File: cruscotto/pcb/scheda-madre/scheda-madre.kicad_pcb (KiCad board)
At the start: 2 copper layers, 178.7 x 74 mm, 13 parts, among them J1 Micro-Fit 2x12 verso auto (D-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

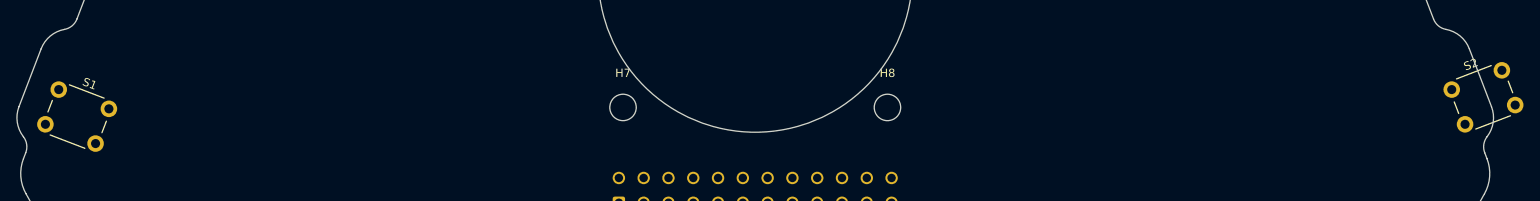
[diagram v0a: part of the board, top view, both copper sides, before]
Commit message: fix(pcb): switches centred under the original buttons and rotated with pins parallel to the edge
The footprint origin is pin 1, so the right switch body fell outside the board. DRC 0 violations; courtyard corners overhang the edge by ~0.5 mm.

Co-Authored-By: Claude Opus 5.5 <noreply@anthropic.com>
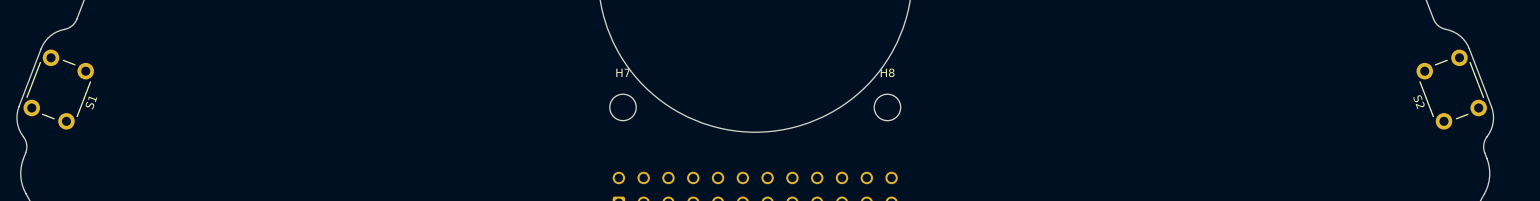
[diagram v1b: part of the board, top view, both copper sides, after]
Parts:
- moved S2 3.95 mm to (231.8, 122.7), turned to 111 degrees
- moved S1 3.95 mm to (67.5, 116.6), turned to -111 degrees

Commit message: feat(pcb): netlist import and preliminary block placement of all 139 parts on both sides
Nets from the schematic via kicad-cli; placement checks outline, holes, fan, overlaps and through-hole pins on both faces. ESP32 radio unused: body-only courtyard. Design rules in the project file. DRC: only unrouted connections.

Co-Authored-By: Claude Opus 5.5 <noreply@anthropic.com>
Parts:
- added BT1: CR2032, BatteryHolder_Keystone_3034_1x20mm, B.Cu at (182.1, 89.5)
- added C1: 100nF 100V, C_0805_2012Metric_Pad1.18x1.45mm_HandSolder, F.Cu at (111.6, 75.5)
- added C10: 39pF, C_0805_2012Metric_Pad1.18x1.45mm_HandSolder, F.Cu at (111.6, 116.0)
- added C11: 2.2uF 100V, C_1210_3225Metric_Pad1.33x2.70mm_HandSolder, F.Cu at (92.5, 111.6)
- added C12: 220nF 100V, C_0805_2012Metric_Pad1.18x1.45mm_HandSolder, F.Cu at (111.6, 119.0)
- added C13: 1uF, C_0805_2012Metric_Pad1.18x1.45mm_HandSolder, F.Cu at (111.6, 122.0)
- added C14: 100nF, C_0805_2012Metric_Pad1.18x1.45mm_HandSolder, F.Cu at (126.1, 122.5)
- added C15: 22uF 10V, C_1206_3216Metric_Pad1.33x1.80mm_HandSolder, F.Cu at (86.5, 111.2)
- added C16: 22uF 10V, C_1206_3216Metric_Pad1.33x1.80mm_HandSolder, F.Cu at (80.5, 112.7)
- added C17: 22uF 10V, C_1206_3216Metric_Pad1.33x1.80mm_HandSolder, F.Cu at (111.0, 113.2)
- added C18: 100nF, C_0805_2012Metric_Pad1.18x1.45mm_HandSolder, F.Cu at (121.6, 122.5)
- added C19: 100nF, C_0805_2012Metric_Pad1.18x1.45mm_HandSolder, F.Cu at (117.1, 122.5)
- added C2: 100nF 25V, C_0805_2012Metric_Pad1.18x1.45mm_HandSolder, F.Cu at (126.1, 86.0)
- added C20: 22uF 10V, C_1206_3216Metric_Pad1.33x1.80mm_HandSolder, F.Cu at (145.0, 79.2)
- added C21: 100nF, C_0805_2012Metric_Pad1.18x1.45mm_HandSolder, F.Cu at (163.6, 79.5)
- added C22: 1uF, C_0805_2012Metric_Pad1.18x1.45mm_HandSolder, F.Cu at (192.1, 80.0)
- added C23: 100nF, C_0805_2012Metric_Pad1.18x1.45mm_HandSolder, F.Cu at (150.1, 80.5)
- added C24: 100nF, C_0805_2012Metric_Pad1.18x1.45mm_HandSolder, F.Cu at (168.1, 80.5)
- added C25: 1uF, C_0805_2012Metric_Pad1.18x1.45mm_HandSolder, F.Cu at (149.6, 70.0)
- added C26: 1uF, C_0805_2012Metric_Pad1.18x1.45mm_HandSolder, F.Cu at (154.1, 70.0)
- added C27: 100nF, C_0805_2012Metric_Pad1.18x1.45mm_HandSolder, F.Cu at (170.6, 70.0)
- added C28: 100nF, C_0805_2012Metric_Pad1.18x1.45mm_HandSolder, F.Cu at (218.6, 109.0)
- added C29: 10uF 16V, CP_Elec_4x5.4, F.Cu at (212.6, 106.4)
- added C3: 220uF 50V, CP_Radial_D10.0mm_P5.00mm, B.Cu at (93.7, 96.3)
- added C30: 100nF, C_0805_2012Metric_Pad1.18x1.45mm_HandSolder, F.Cu at (216.6, 112.0)
- added C31: 1uF, C_0805_2012Metric_Pad1.18x1.45mm_HandSolder, F.Cu at (211.1, 113.5)
- added C32: 1uF, C_0805_2012Metric_Pad1.18x1.45mm_HandSolder, F.Cu at (180.6, 114.0)
- added C33: 100nF, C_0805_2012Metric_Pad1.18x1.45mm_HandSolder, F.Cu at (180.1, 81.5)
- added C34: 100nF, C_0805_2012Metric_Pad1.18x1.45mm_HandSolder, B.Cu at (111.6, 75.5)
- added C35: 10uF, C_1206_3216Metric_Pad1.33x1.80mm_HandSolder, F.Cu at (158.5, 79.7)
- added C36: 100nF, C_0805_2012Metric_Pad1.18x1.45mm_HandSolder, F.Cu at (184.6, 81.5)
- added C4: 2.2uF 100V, C_1210_3225Metric_Pad1.33x2.70mm_HandSolder, F.Cu at (107.0, 79.6)
- added C5: 2.2uF 100V, C_1210_3225Metric_Pad1.33x2.70mm_HandSolder, F.Cu at (95.0, 88.1)
- added C6: 100nF, C_0805_2012Metric_Pad1.18x1.45mm_HandSolder, F.Cu at (126.1, 89.0)
- added C7: 47uF 10V, C_1210_3225Metric_Pad1.33x2.70mm_HandSolder, F.Cu at (82.5, 96.6)
- added C8: 47uF 10V, C_1210_3225Metric_Pad1.33x2.70mm_HandSolder, F.Cu at (98.5, 110.6)
- added C9: 6.8nF, C_0805_2012Metric_Pad1.18x1.45mm_HandSolder, F.Cu at (126.1, 99.0)
- added D1: SMCJ26CA, D_SMC, F.Cu at (104.6, 93.9)
- added D10: NUP2105L, SOT-23, F.Cu at (185.0, 110.2)
- added D11: 1N4148W, D_SOD-123, B.Cu at (94.1, 88.2)
- added D12: 1N4148W, D_SOD-123, B.Cu at (185.6, 76.2)
- added D13: B340A, D_SMA, F.Cu at (186.0, 77.8)
- added D2: B560C, D_SMC, F.Cu at (104.6, 101.4)
- added D3: 1N4148W, D_SOD-123, F.Cu at (105.1, 113.2)
- added D4: BAT54J, D_SOD-323F, F.Cu at (125.9, 102.0)
- added D5: BAT54S, SOT-23, F.Cu at (126.5, 95.2)
- added D6: BAT54S, SOT-23, F.Cu at (79.5, 108.7)
- added D7: verde, LED_0805_2012Metric_Pad1.15x1.40mm_HandSolder, F.Cu at (144.1, 82.0)
- added D8: SMBJ26CA, D_SMB, F.Cu at (181.3, 105.3)
- added D9: 1N4148W, D_SOD-123, F.Cu at (211.6, 110.7)
- added FB1: ferrite >= 3A, 1206, L_1206_3216Metric_Pad1.22x1.90mm_HandSolder, F.Cu at (82.4, 100.2)
- added J10: Verso P1 S3: 5V TXD RXD GND, Molex_PicoBlade_53047-0410_1x04_P1.25mm_Vertical, F.Cu at (209.0, 137.9)
- added J11: Verso P2 S3: IO19 IO11 IO12 IO13, Molex_PicoBlade_53047-0410_1x04_P1.25mm_Vertical, F.Cu at (174.6, 137.5)
- added J12: Verso P6 Speak S3, Molex_PicoBlade_53047-0210_1x02_P1.25mm_Vertical, F.Cu at (191.9, 137.5)
- added J3: USB-C (solo a banco), USB_C_Receptacle_HRO_TYPE-C-31-M-12, F.Cu at (162.5, 73.6)
- added J4: Ventola Delta AFB0412VA-00 (D-052), FanPinHeader_1x04_P2.54mm_Vertical, B.Cu at (174.2, 117.2)
- added J5: NTC display, JST_XH_B2B-XH-A_1x02_P2.50mm_Vertical, F.Cu at (136.0, 79.4)
- added J6: STEVAL-MKI196V1 (DIL-24), ST_DIL24_Adapter_W15.0mm, B.Cu at (78.0, 117.0)
- added J7: Modulo MicroSD: 3V3 CS MOSI CLK MISO GND, PinHeader_1x06_P2.54mm_Vertical, F.Cu at (223.2, 110.3)
- added J8: Modulo VAN: 3.3V GND RX TX, PinHeader_1x04_P2.54mm_Vertical, B.Cu at (211.2, 93.8)
- added J9: Modulo VAN: CANH CANL, PinHeader_1x02_P2.54mm_Vertical, B.Cu at (196.7, 83.8)
- added K1: G2RL-2 DC5, Relay_DPDT_Omron_G2RL-2, B.Cu at (120.7, 80.1)
- added K2: G2RL-2 DC5, Relay_DPDT_Omron_G2RL-2, B.Cu at (205.9, 126.8)
- added L1: 8.2uH Isat>=5A, L_Bourns_SRR1260, F.Cu at (121.0, 114.0)
- added L2: 22uH Isat>=1.5A, L_Bourns_SRN6045TA, F.Cu at (86.0, 105.8)
- added Q1: IPD50N06S4L-12 (da confermare), TO-252-2, F.Cu at (104.7, 86.0)
- added Q3: ZXMP6A13F (P 60 V), SOT-23, F.Cu at (153.0, 76.7)
- added Q4: MMBTA06 (80 V), SOT-23, F.Cu at (170.5, 76.7)
- added Q5: MMBT3904, SOT-23, F.Cu at (175.5, 79.2)
- added Q6: MMBT3904, SOT-23, F.Cu at (140.0, 70.7)
- added Q7: MMBT3904, SOT-23, F.Cu at (145.0, 70.7)
- added Q8: MMBT5551, SOT-23, F.Cu at (171.0, 111.2)
- added Q9: AO3400A, SOT-23, B.Cu at (107.5, 79.2)
- added R1: 53.6k, R_0805_2012Metric_Pad1.20x1.40mm_HandSolder, F.Cu at (112.6, 125.0)
- added R10: 43.2k, R_0805_2012Metric_Pad1.20x1.40mm_HandSolder, F.Cu at (125.1, 131.5)
- added R11: 100k, R_0805_2012Metric_Pad1.20x1.40mm_HandSolder, F.Cu at (120.6, 131.5)
- added R12: 22k, R_0805_2012Metric_Pad1.20x1.40mm_HandSolder, F.Cu at (116.1, 134.0)
- added R13: 470k, R_0805_2012Metric_Pad1.20x1.40mm_HandSolder, F.Cu at (111.6, 134.0)
- added R14: 100k, R_0805_2012Metric_Pad1.20x1.40mm_HandSolder, F.Cu at (125.1, 134.5)
- added R15: 10k, R_0805_2012Metric_Pad1.20x1.40mm_HandSolder, F.Cu at (154.6, 82.5)
- added R16: 10k, R_0805_2012Metric_Pad1.20x1.40mm_HandSolder, F.Cu at (159.1, 82.5)
- added R17: 1k, R_0805_2012Metric_Pad1.20x1.40mm_HandSolder, F.Cu at (163.6, 82.5)
- added R18: 4.7k, R_0805_2012Metric_Pad1.20x1.40mm_HandSolder, F.Cu at (172.6, 83.0)
- added R19: 4.7k, R_0805_2012Metric_Pad1.20x1.40mm_HandSolder, F.Cu at (189.1, 83.0)
- added R2: 10.2k, R_0805_2012Metric_Pad1.20x1.40mm_HandSolder, F.Cu at (126.1, 125.5)
- added R20: 1k, R_0805_2012Metric_Pad1.20x1.40mm_HandSolder, F.Cu at (168.1, 83.5)
- added R21: 1k, R_0805_2012Metric_Pad1.20x1.40mm_HandSolder, F.Cu at (177.1, 84.5)
- added R22: 100k, R_0805_2012Metric_Pad1.20x1.40mm_HandSolder, F.Cu at (181.6, 84.5)
- added R23: 100k, R_0805_2012Metric_Pad1.20x1.40mm_HandSolder, F.Cu at (172.6, 86.0)
- added R24: 6.8k, R_0805_2012Metric_Pad1.20x1.40mm_HandSolder, F.Cu at (186.1, 86.0)
- added R25: 10k, R_0805_2012Metric_Pad1.20x1.40mm_HandSolder, F.Cu at (190.6, 86.0)
- added R26: 10k, R_0805_2012Metric_Pad1.20x1.40mm_HandSolder, F.Cu at (201.1, 86.5)
- added R27: 100k, R_0805_2012Metric_Pad1.20x1.40mm_HandSolder, F.Cu at (177.1, 87.5)
- added R28: 10k, R_0805_2012Metric_Pad1.20x1.40mm_HandSolder, F.Cu at (181.6, 87.5)
- added R29: 1k, R_0805_2012Metric_Pad1.20x1.40mm_HandSolder, F.Cu at (170.6, 89.0)
- added R3: 162k, R_0805_2012Metric_Pad1.20x1.40mm_HandSolder, F.Cu at (121.6, 125.5)
- added R30: 1k, R_0805_2012Metric_Pad1.20x1.40mm_HandSolder, F.Cu at (186.1, 89.0)
- added R31: 5.1k, R_0805_2012Metric_Pad1.20x1.40mm_HandSolder, F.Cu at (149.6, 73.0)
- added R32: 5.1k, R_0805_2012Metric_Pad1.20x1.40mm_HandSolder, F.Cu at (154.1, 73.0)
- added R33: 4.7k, R_0805_2012Metric_Pad1.20x1.40mm_HandSolder, F.Cu at (170.6, 73.0)
- added R34: 4.7k, R_0805_2012Metric_Pad1.20x1.40mm_HandSolder, F.Cu at (134.6, 74.5)
- added R35: 10k, R_0805_2012Metric_Pad1.20x1.40mm_HandSolder, F.Cu at (143.6, 74.5)
- added R36: 10k, R_0805_2012Metric_Pad1.20x1.40mm_HandSolder, F.Cu at (148.1, 76.0)
- added R37: 0, R_0805_2012Metric_Pad1.20x1.40mm_HandSolder, F.Cu at (139.1, 74.5)
- added R38: 330, R_0805_2012Metric_Pad1.20x1.40mm_HandSolder, F.Cu at (185.1, 114.0)
- added R39: 47k, R_0805_2012Metric_Pad1.20x1.40mm_HandSolder, F.Cu at (215.6, 115.0)
- added R4: 13.0k, R_0805_2012Metric_Pad1.20x1.40mm_HandSolder, F.Cu at (117.1, 125.5)
- added R40: 68k, R_0805_2012Metric_Pad1.20x1.40mm_HandSolder, F.Cu at (211.1, 116.5)
- added R41: 10k, R_0805_2012Metric_Pad1.20x1.40mm_HandSolder, F.Cu at (215.6, 118.0)
- added R42: 150k, R_0805_2012Metric_Pad1.20x1.40mm_HandSolder, F.Cu at (211.1, 119.5)
- added R43: 10k, R_0805_2012Metric_Pad1.20x1.40mm_HandSolder, F.Cu at (215.6, 121.0)
- added R44: 330k, R_0805_2012Metric_Pad1.20x1.40mm_HandSolder, F.Cu at (211.1, 122.5)
- added R45: 4.7k, R_0805_2012Metric_Pad1.20x1.40mm_HandSolder, F.Cu at (215.6, 124.0)
- added R46: 1k, R_0805_2012Metric_Pad1.20x1.40mm_HandSolder, F.Cu at (211.1, 125.5)
- added R47: 100k, R_0805_2012Metric_Pad1.20x1.40mm_HandSolder, F.Cu at (215.6, 127.0)
- added R49: 10k, R_0805_2012Metric_Pad1.20x1.40mm_HandSolder, F.Cu at (179.6, 90.5)
- added R5: 523k, R_0805_2012Metric_Pad1.20x1.40mm_HandSolder, F.Cu at (112.6, 128.0)
- added R54: 100, R_0805_2012Metric_Pad1.20x1.40mm_HandSolder, B.Cu at (83.1, 95.0)
- added R55: 100k, R_0805_2012Metric_Pad1.20x1.40mm_HandSolder, B.Cu at (107.6, 95.5)
- added R56: 10k, R_0805_2012Metric_Pad1.20x1.40mm_HandSolder, F.Cu at (170.6, 92.0)
- added R6: 84.5k, R_0805_2012Metric_Pad1.20x1.40mm_HandSolder, F.Cu at (125.1, 128.5)
- added R7: 10k, R_0805_2012Metric_Pad1.20x1.40mm_HandSolder, F.Cu at (120.6, 128.5)
- added R8: 100k, R_0805_2012Metric_Pad1.20x1.40mm_HandSolder, F.Cu at (116.1, 131.0)
- added R9: 100k, R_0805_2012Metric_Pad1.20x1.40mm_HandSolder, F.Cu at (111.6, 131.0)
- added RT1: NTC 100k B3950, R_0805_2012Metric_Pad1.20x1.40mm_HandSolder, F.Cu at (175.1, 90.5)
- added SW3: RESET, SW_PUSH_6mm, F.Cu at (213.0, 130.5)
- added SW4: BOOT, SW_PUSH_6mm, F.Cu at (197.5, 132.0)
- added U1: LM74700-Q1, SOT-23-6, F.Cu at (126.4, 82.2)
- added U10: DS3231SN, SOIC-16W_7.5x10.3mm_P1.27mm, B.Cu at (103.5, 88.4)
- added U2: TPS54360B, TI_SO-PowerPAD-8_ThermalVias, F.Cu at (105.7, 108.3)
- added U3: LMR36510, Texas_HTSOP-8-1EP_3.9x4.9mm_P1.27mm_EP2.95x4.9mm_Mask2.4x3.1mm_ThermalVias, F.Cu at (94.8, 105.3)
- added U4: ESP32-WROOM-32E-H4, ESP32-WROOM-32E, F.Cu at (198.9, 102.3)
- added U5: AP2112K-3.3, SOT-23-5, F.Cu at (134.9, 70.7)
- added U6: CH340C, SOIC-16_3.9x9.9mm_P1.27mm, F.Cu at (128.3, 74.2)
- added U7: LM2903B, SOIC-8_3.9x4.9mm_P1.27mm, F.Cu at (173.3, 105.7)
- added U9: AP2112K-3.3, SOT-23-5, F.Cu at (179.9, 110.2)
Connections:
- J1 pad 1: (no net) -> VBAT_IN
- J1 pad 10: (no net) -> SPK_L_P
- J1 pad 11: (no net) -> SPK_L_N
- J1 pad 12: (no net) -> RADIO_R_P
- J1 pad 13: (no net) -> RADIO_R_N
- J1 pad 14: (no net) -> SPK_R_P
- J1 pad 15: (no net) -> SPK_R_N
- J1 pad 2: (no net) -> GND
- J1 pad 3: (no net) -> KEY_IN
- J1 pad 4: (no net) -> KLINE
- J1 pad 5: (no net) -> VAN_DATA
- J1 pad 6: (no net) -> VAN_DATAB
- J1 pad 7: (no net) -> VAN_GND_REF
- J1 pad 8: (no net) -> RADIO_L_P
- J1 pad 9: (no net) -> RADIO_L_N
- S1 pad 1: (no net) -> GND
- S1 pad 2: (no net) -> S3_IO19
- S2 pad 1: (no net) -> GND
- S2 pad 2: (no net) -> FE_BTN2

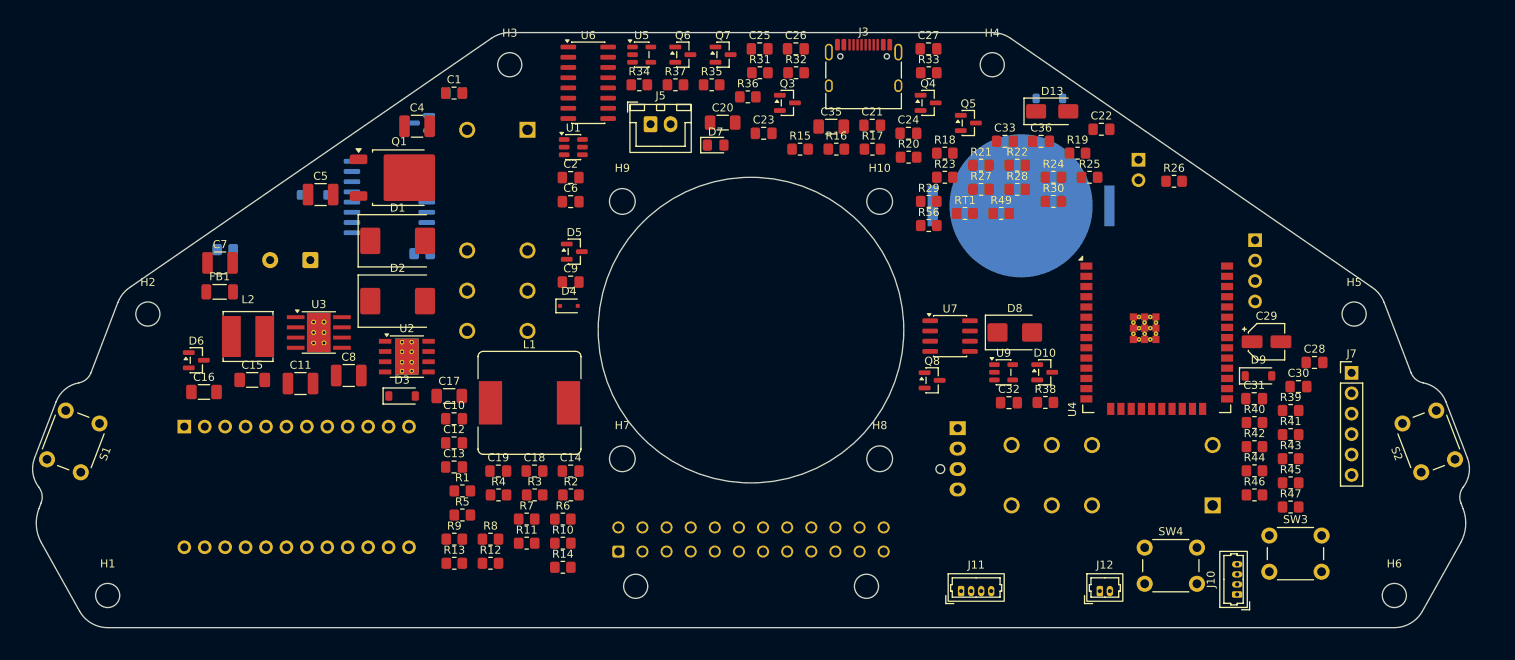
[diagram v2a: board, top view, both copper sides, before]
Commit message: feat(pcb): S3 cable connectors mirrored to face their S3 counterparts, right-angle PicoBlade; height check
KiCad F view is the mirror of the user's DXF (seen from the rear): S3-related parts placed at negative x. Right-angle PicoBlade 53048 keeps plugs flat. Clearance to the S3 at least 5.5 mm on face F. Relays moved to the left back, IMU socket to the right.

Co-Authored-By: Claude Opus 5.5 <noreply@anthropic.com>
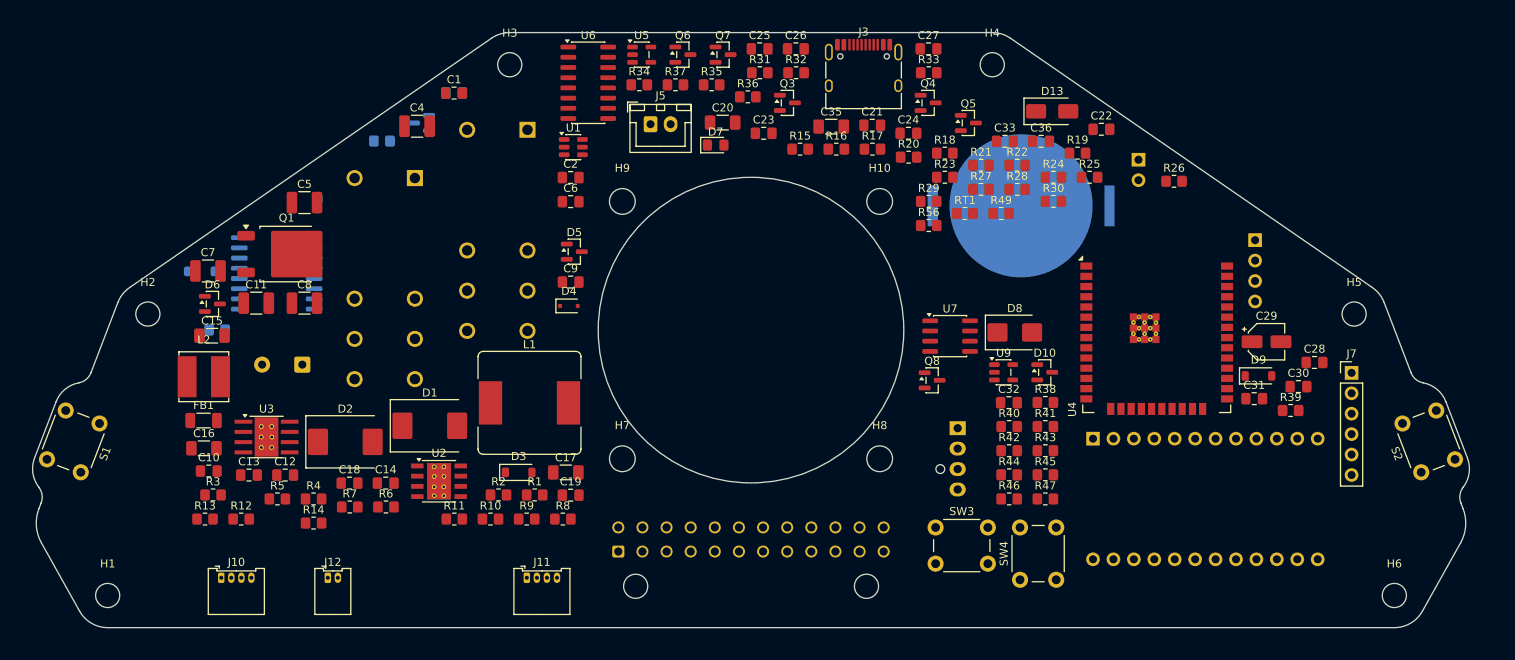
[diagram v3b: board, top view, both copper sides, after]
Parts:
- J10, J11: footprint Molex_PicoBlade_53047-0410_1x04_P1.25mm_Vertical -> Molex_PicoBlade_53048-0410_1x04_P1.25mm_Horizontal
- J12: footprint Molex_PicoBlade_53047-0210_1x02_P1.25mm_Vertical -> Molex_PicoBlade_53048-0210_1x02_P1.25mm_Horizontal
- moved J10 126.3 mm to (82.6, 135.8), turned to 0 degrees
- moved J6 113.0 mm to (191.0, 118.5)
- moved D12 107.7 mm to (80.1, 97.7)
- moved K2 107.2 mm to (106.7, 86.1), turned to 180 degrees
- moved J12 96.0 mm to (95.9, 135.8)
- moved J11 54.0 mm to (120.6, 135.8)
- moved SW3 41.5 mm to (171.5, 129.5)
- moved R3 40.0 mm to (81.6, 125.5)
- moved R12 31.5 mm to (85.1, 128.5)
- moved R13 31.5 mm to (80.6, 128.5)
- moved R14 31.5 mm to (94.1, 129.0)
- moved C10 31.2 mm to (81.1, 122.5)
- moved R41 30.5 mm to (185.1, 117.0)
- moved R43 30.5 mm to (185.1, 120.0)
- moved R45 30.5 mm to (185.1, 123.0)
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
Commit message: feat(pcb): first automatic routing draft with Freerouting (71 connections unrouted, not usable yet)
Routing script with net classes, ground planes on both faces, Specctra round trip through Freerouting 2.5.0 on Java 25. Placement regenerated without the RTC coin cell (D-056). DRC findings recorded in the PCB README.

Co-Authored-By: Claude Opus 5.5 <noreply@anthropic.com>
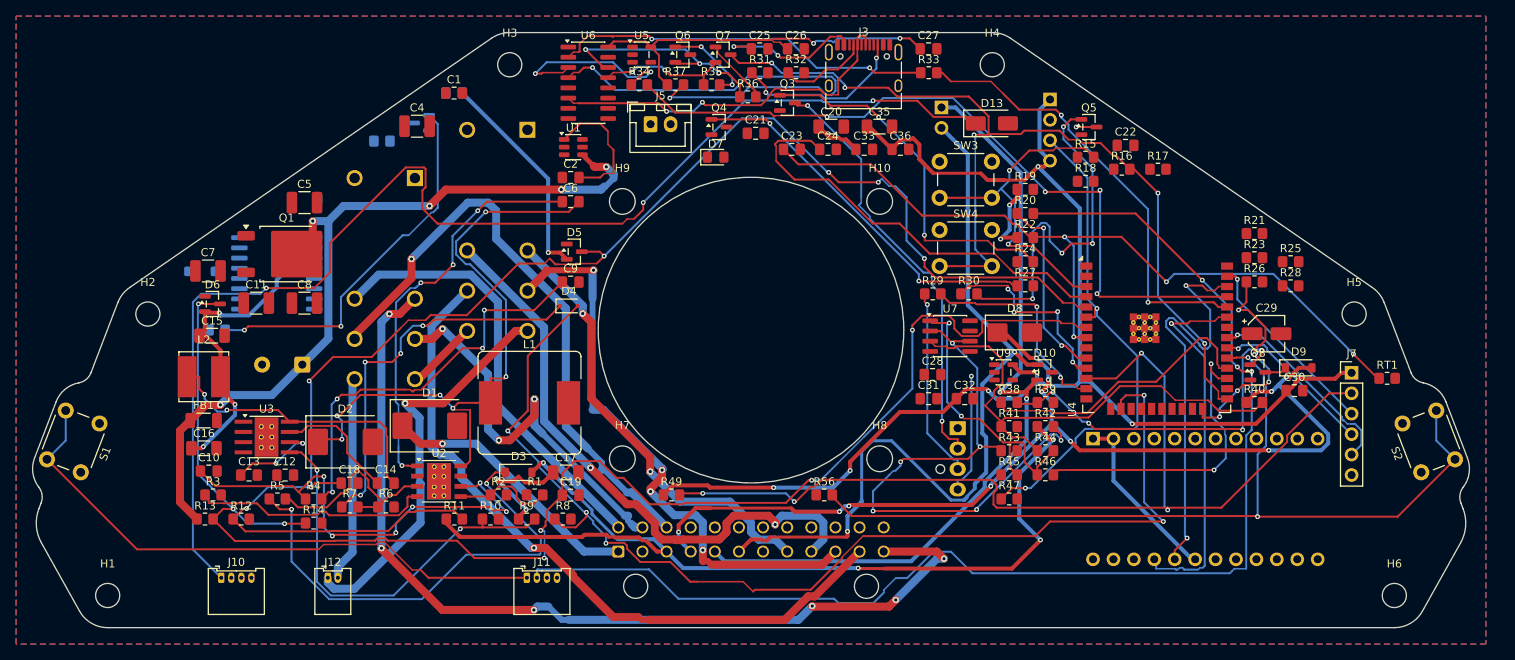
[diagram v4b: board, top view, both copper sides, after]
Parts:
- removed BT1: CR2032, BatteryHolder_Keystone_3034_1x20mm
- moved RT1 56.4 mm to (227.6, 111.0)
- moved R49 53.9 mm to (138.6, 125.5)
- moved C28 47.5 mm to (171.1, 110.5)
- moved SW3 45.5 mm to (172.0, 84.0)
- moved SW4 44.6 mm to (172.0, 92.5), turned to 0 degrees
- moved Q8 40.5 mm to (211.5, 110.2)
- moved C31 40.5 mm to (170.6, 113.5)
- moved R23 39.8 mm to (211.1, 96.0)
- moved R28 36.1 mm to (215.6, 99.5)
- moved R56 35.9 mm to (157.6, 125.5)
- moved R16 35.6 mm to (194.6, 85.0)
- moved R17 35.6 mm to (199.1, 85.0)
- moved R15 35.5 mm to (190.1, 83.5)
- moved R21 35.0 mm to (211.1, 93.0)
- moved J8 30.9 mm to (185.7, 76.3)
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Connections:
- U10 pad 14: Net-(BT1-+) -> GND
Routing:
- net KEY_SENSE: track 0.00 -> 186.9 mm, vias 0 -> 7
- net VBAT_SENSE: track 0.00 -> 184.5 mm, vias 0 -> 7
- net +3V3_SW: track 0.00 -> 169.8 mm, vias 0 -> 6
- net LINK_FE2S3: track 0.00 -> 159.0 mm, vias 0 -> 3
- net Net-(D13-K): track 0.00 -> 156.7 mm, vias 0 -> 3
- net PWR_HOLD: track 0.00 -> 140.5 mm, vias 0 -> 5
- net KLINE: track 0.00 -> 127.7 mm, vias 0 -> 11
- net SD_CS: track 0.00 -> 124.3 mm, vias 0 -> 4
- net +3V3_AON: track 0.00 -> 119.5 mm, vias 0 -> 8
- net KEY_IN: track 0.00 -> 118.6 mm, vias 0 -> 4
- net RADIO_R_P: track 0.00 -> 118.6 mm, vias 0 -> 6
- net FE_IO0: track 0.00 -> 117.5 mm, vias 0 -> 5
- net FE_BTN2: track 0.00 -> 112.5 mm, vias 0 -> 2
- net NTC_PCB: track 0.00 -> 101.6 mm, vias 0 -> 4
- net VBAT_P: track 0.00 -> 99.6 mm, vias 0 -> 5
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- added copper zone on B.Cu, net GND
- added copper zone on F.Cu, net GND
